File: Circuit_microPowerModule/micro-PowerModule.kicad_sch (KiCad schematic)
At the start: 3 parts, among them J2 Jack-DC, J3 Screw_Terminal_01x02

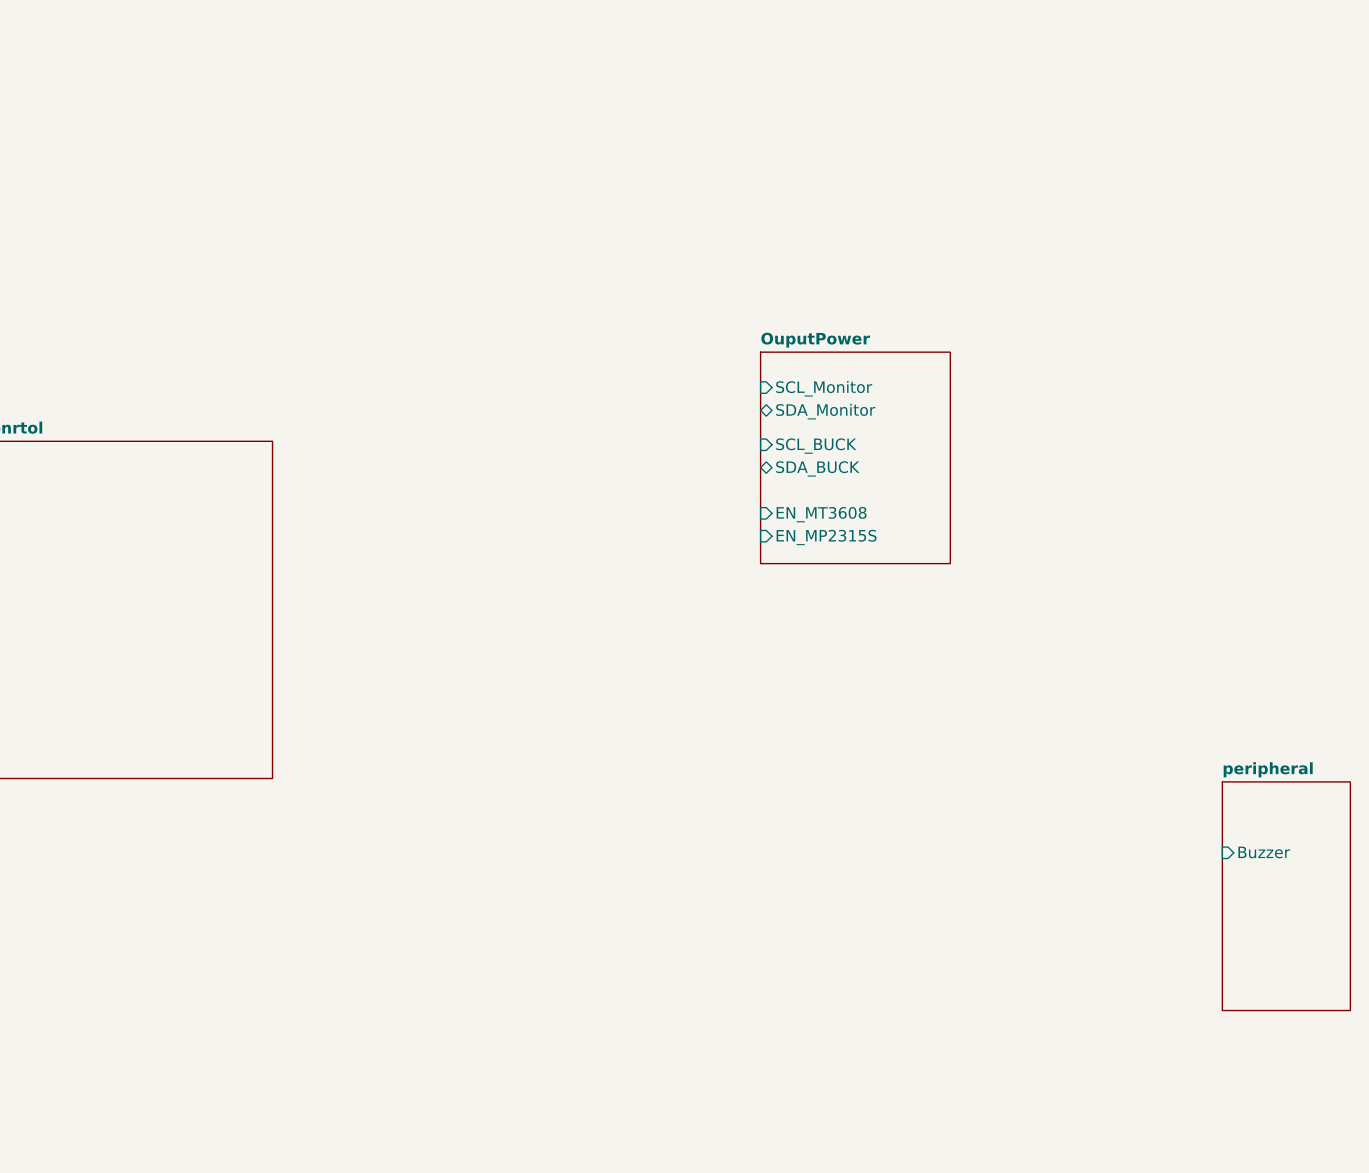
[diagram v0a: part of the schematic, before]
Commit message: added mikrobus header
added filter capacitance, I2C pull-up resistor
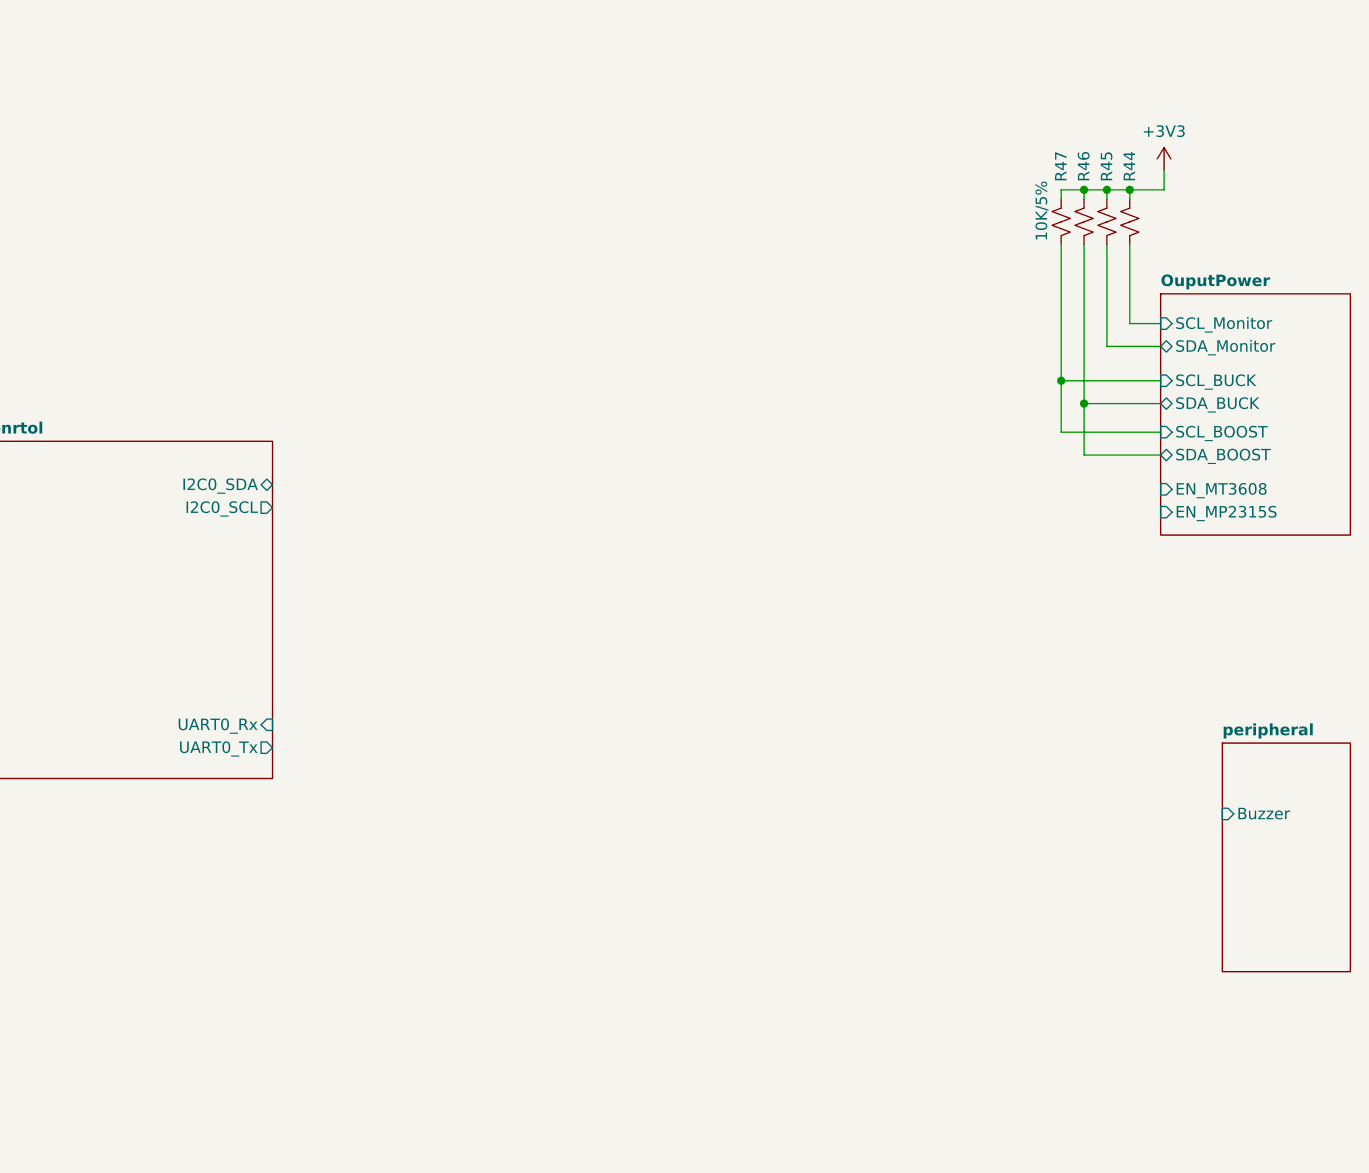
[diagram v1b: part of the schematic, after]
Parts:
- added R44, R45, R46, R47: 10K/5%, Resistor_SMD:R_0603_1608Metric, symbol Device:R_Small_US
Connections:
- net OuputPower/SCL_Monitor: now also R44.2
- net OuputPower/SDA_Monitor: now also R45.2
- new net +3V3: R44.1, R45.1, R46.1, R47.1
- new net OuputPower/SCL_BOOST: R47.2
- new net OuputPower/SDA_BOOST: R46.2
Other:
- sheet OuputPower ports: added SCL_BOOST, SDA_BOOST; removed none
- sheet main_conrtol ports: added I2C0_SCL, I2C0_SDA, UART0_Rx, UART0_Tx; removed none

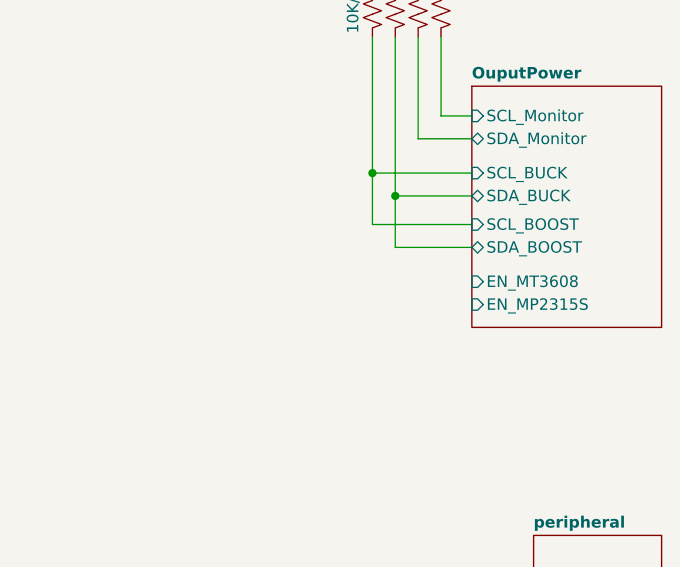
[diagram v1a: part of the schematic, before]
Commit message: added Nokia 5110 LCD symbol
linked some component pin
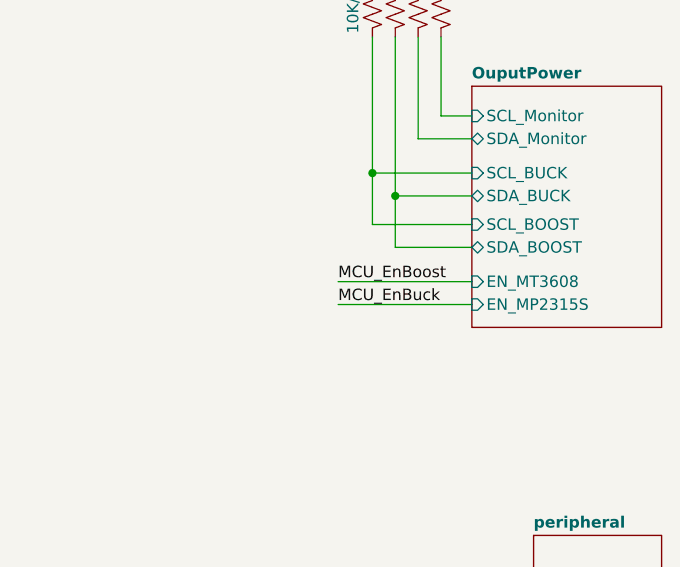
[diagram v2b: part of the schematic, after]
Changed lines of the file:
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@@
     (stroke (width 0) (type default))
   )
+  (wire (pts (xy 248.92 84.328) (xy 263.779 84.328))
+    (stroke (width 0) (type default))
+  )
   (wire (pts (xy 255.27 72.263) (xy 263.779 72.263))
+    (stroke (width 0) (type default))
+  )
+  (wire (pts (xy 248.92 81.788) (xy 263.779 81.788))
     (stroke (width 0) (type default))
   )
@@
     (effects (font (size 1.27 1.27)) (justify right bottom))
   )
+  (label "MCU_EnBuck" (at 248.92 84.328 0) (fields_autoplaced)
+    (effects (font (size 1.27 1.27)) (justify left bottom))
+  )
+  (label "MCU_EnBoost" (at 248.92 81.788 0) (fields_autoplaced)
+    (effects (font (size 1.27 1.27)) (justify left bottom))
+  )
   (label "PWR_IN" (at 69.215 35.941 180) (fields_autoplaced)

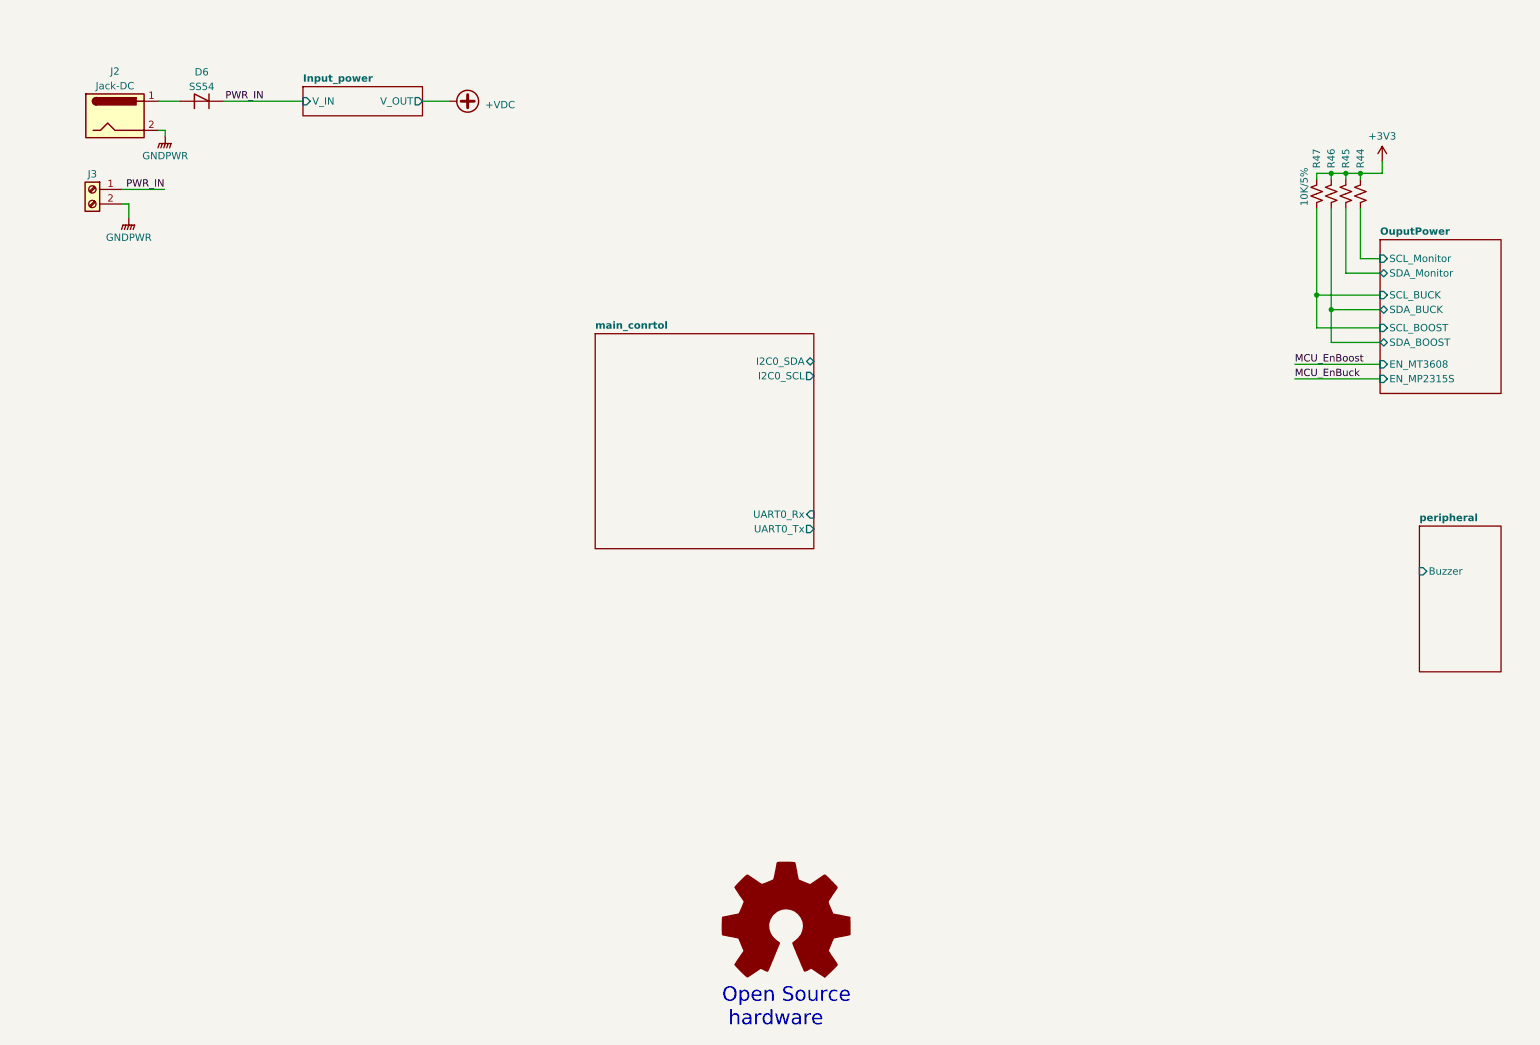
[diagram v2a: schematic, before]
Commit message: added schematic svg file
added encoder wire, mikrobus connect
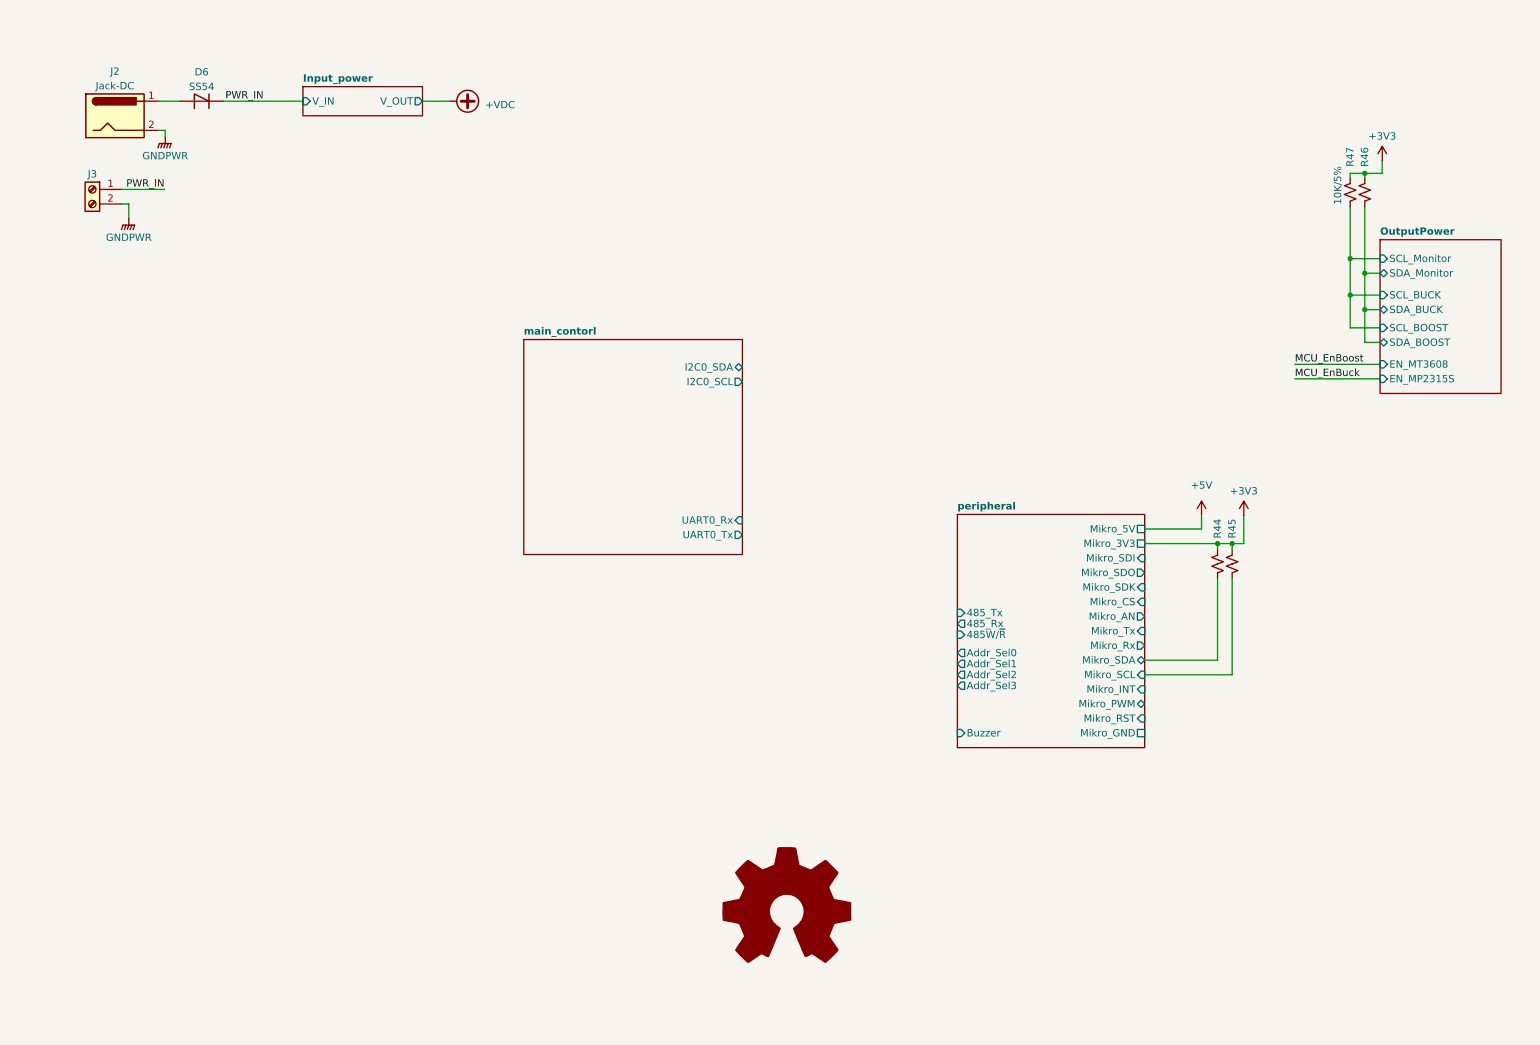
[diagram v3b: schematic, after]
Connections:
- net OutputPower/SCL_Monitor renamed peripheral/Mikro_SDA
- net OutputPower/SDA_Monitor renamed peripheral/Mikro_SCL
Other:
- sheet OuputPower renamed OutputPower
- sheet main_conrtol renamed main_contorl
- sheet peripheral ports: added 485W/~{R}, 485_Rx, 485_Tx, Addr_Sel0, Addr_Sel1, Addr_Sel2, Addr_Sel3, Mikro_3V3, Mikro_5V, Mikro_AN, Mikro_CS, Mikro_GND, Mikro_INT, Mikro_PWM, Mikro_RST, Mikro_Rx, Mikro_SCL, Mikro_SDA, Mikro_SDI, Mikro_SDK, Mikro_SDO, Mikro_Tx; removed none
- note removed: "Open Source hardware"
- moved on the sheet: R46, R47

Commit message: define mcu pinout to mikrobus
update hw block diagram file type
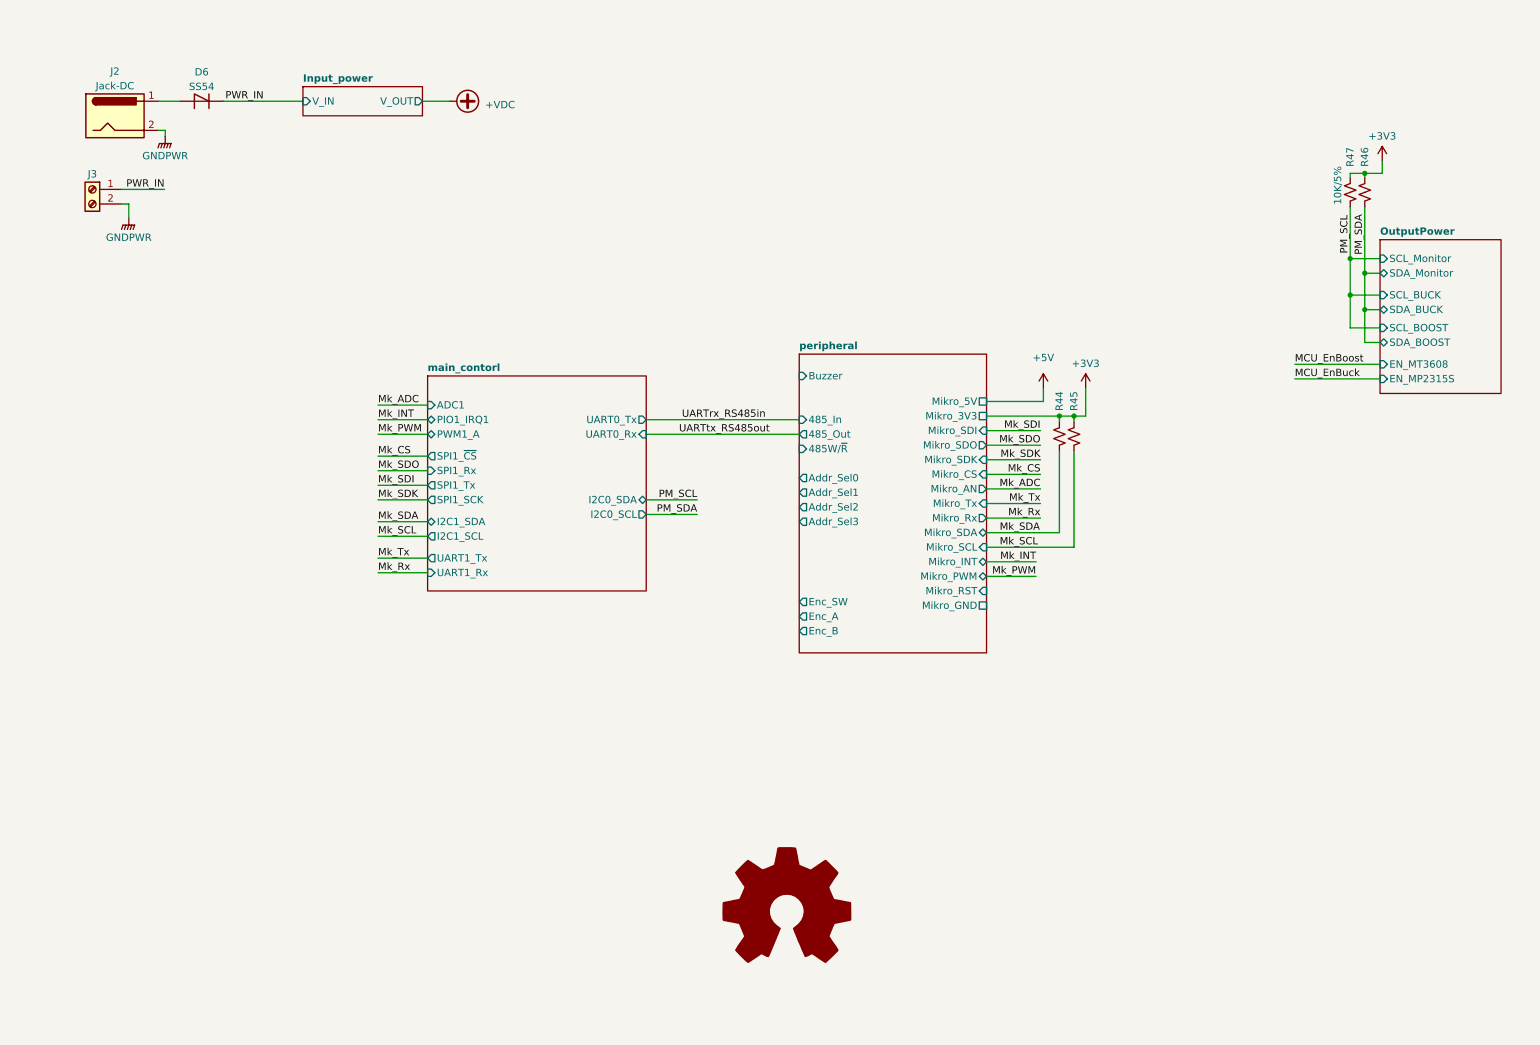
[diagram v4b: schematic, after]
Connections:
- net OutputPower/SCL_BOOST renamed PM_SCL
- net OutputPower/SDA_BOOST renamed PM_SDA
- net peripheral/Mikro_SCL renamed Mk_SCL
- net peripheral/Mikro_SDA renamed Mk_SDA
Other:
- sheet main_contorl ports: added ADC1, I2C1_SCL, I2C1_SDA, PIO1_IRQ1, PWM1_A, SPI1_Rx, SPI1_SCK, SPI1_Tx, SPI1_~{CS}, UART1_Rx, UART1_Tx; removed none
- sheet peripheral ports: added 485_In, 485_Out, Enc_A, Enc_B, Enc_SW; removed 485_Rx, 485_Tx
- moved on the sheet: R44, R45
